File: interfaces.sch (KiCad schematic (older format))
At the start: 68 parts, among them J6 0878311420, J7 61300611121, U1 MTFC32GAPALBH-AIT, U14 XC7A100T-FGG484, U17 USB3300-EZK-TR, U18 USB3300-EZK-TR, U6 NVT2008DQ,115, Y1 TSX-3225, Y3 TSX-3225

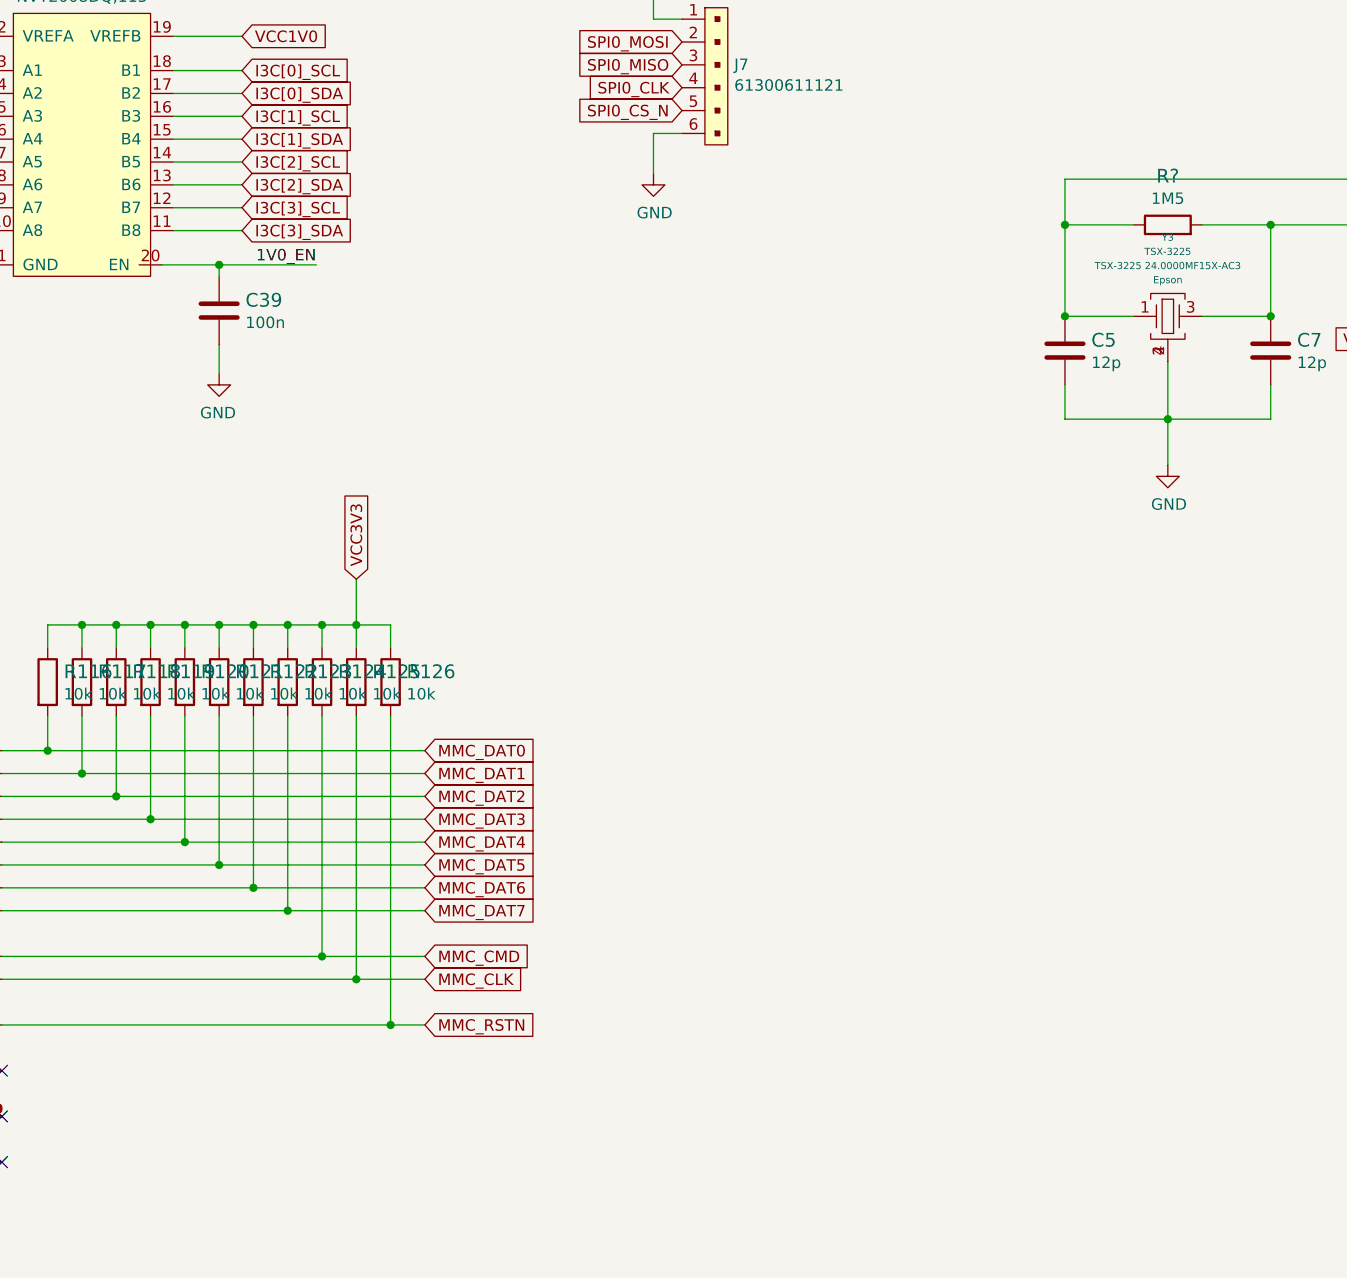
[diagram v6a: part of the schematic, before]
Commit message: Add layout for QSPI1
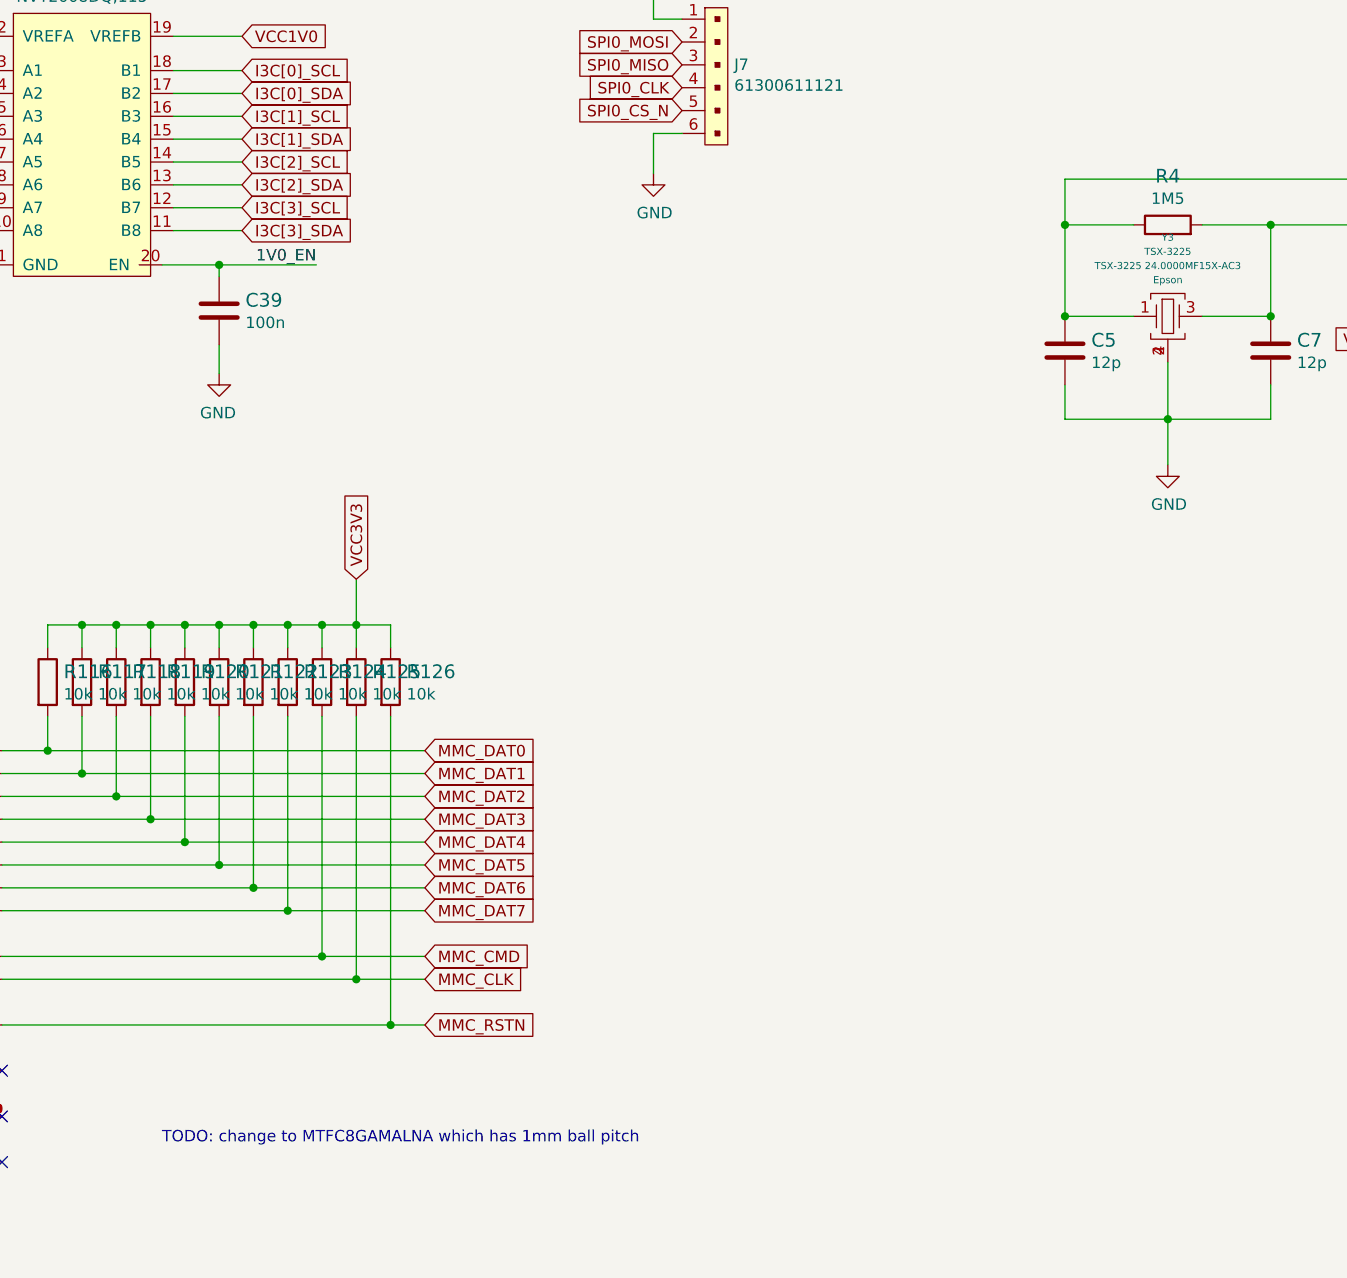
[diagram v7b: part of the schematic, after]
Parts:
- gave numbers to parts that had none: 1
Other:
- note added: "TODO: change to MTFC8GAMALNA which has 1mm ball pitch"
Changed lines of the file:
@@
 TBD: is EXT VBUS, CPEN,  VBUS necessary?\n(datasheet for host variant specifies so)
 $Comp
-L antmicroResistors0402:R_1M5_0402 R?
+L antmicroResistors0402:R_1M5_0402 R4
 U 1 1 603E998C
 P 9750 6600
-F 0 "R?" H 9750 6813 60  0000 C CNN
+F 0 "R4" H 9750 6813 60  0000 C CNN
 F 1 "R_1M5_0402" H 9750 6450 60  0001 C CNN
 F 2 "antmicro-footprints:0402-res" H 9950 6800 60  0001 L CNN
@@
 	1    0    0    -1
 $EndComp
+Text Notes 5350 10625 0    50   ~ 0
+TODO: change to MTFC8GAMALNA which has 1mm ball pitch
 $EndSCHEMATC

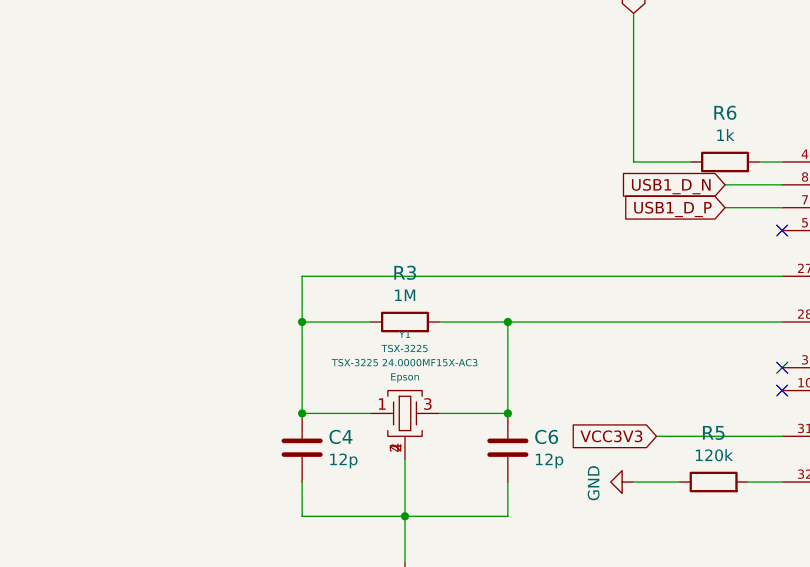
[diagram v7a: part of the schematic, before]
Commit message: Add layout for ULPI USB1
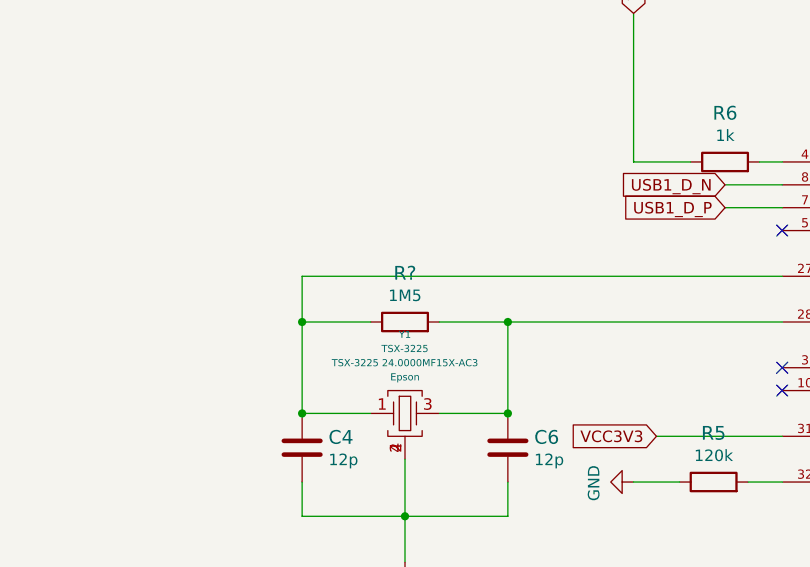
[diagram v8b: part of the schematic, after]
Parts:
- removed R3: R_1M_0603, antmicro-footprints:0603-res, symbol antmicroResistors0603:R_1M_0603
- added R?: R_1M5_0402, antmicro-footprints:0402-res, symbol antmicroResistors0402:R_1M5_0402
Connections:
- net at C4.1, U17.27 (XO), Y1.1: now also R?.1
- net at C6.1, U17.28 (XI), Y1.3: now also R?.2
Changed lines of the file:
@@
-$EndComp
-$Comp
-L antmicroResistors0603:R_1M_0603 R3
-U 1 1 601001C9
-P 9650 3100
-F 0 "R3" H 9650 3313 60  0000 C CNN
-F 1 "R_1M_0603" H 9650 2950 60  0001 C CNN
-F 2 "antmicro-footprints:0603-res" H 9850 3300 60  0001 L CNN
-F 3 "" H 9650 3100 50  0001 C CNN
-F 4 "BOURNS" H 9850 3500 60  0001 L CNN "Manufacturer"
-F 5 "CR0603-JW-105GLF" H 9850 3400 60  0001 L CNN "MPN"
-F 6 "1M" H 9650 3215 50  0000 C CNN "Val"
-	1    9650 3100
-	1    0    0    -1
 $EndComp
 $Comp
@@
 Text Notes 5350 10625 0    50   ~ 0
 TODO: change to MTFC8GAMALNA which has 1mm ball pitch
+$Comp
+L antmicroResistors0402:R_1M5_0402 R?
+U 1 1 60957386
+P 9650 3100
+F 0 "R?" H 9650 3313 60  0000 C CNN
+F 1 "R_1M5_0402" H 9650 2950 60  0001 C CNN
+F 2 "antmicro-footprints:0402-res" H 9850 3300 60  0001 L CNN
+F 3 "" H 9650 3100 50  0001 C CNN
+F 4 "MULTICOMP" H 9850 3500 60  0001 L CNN "Manufacturer"
+F 5 "MCWR04W1504FTL" H 9850 3400 60  0001 L CNN "MPN"
+F 6 "1M5" H 9650 3215 50  0000 C CNN "Val"
+	1    9650 3100
+	1    0    0    -1
+$EndComp
 $EndSCHEMATC
